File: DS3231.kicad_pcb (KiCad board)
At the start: 16 copper layers, 22.9 x 17.8 mm, 14 parts, among them IC1 DS3231/SO

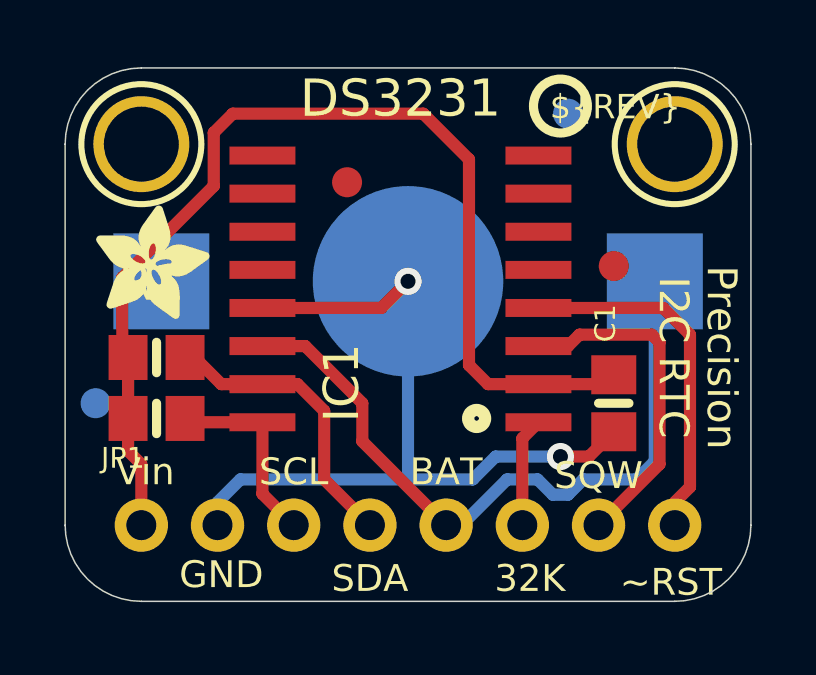
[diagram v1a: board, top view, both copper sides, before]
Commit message: fully migrated to KiCad
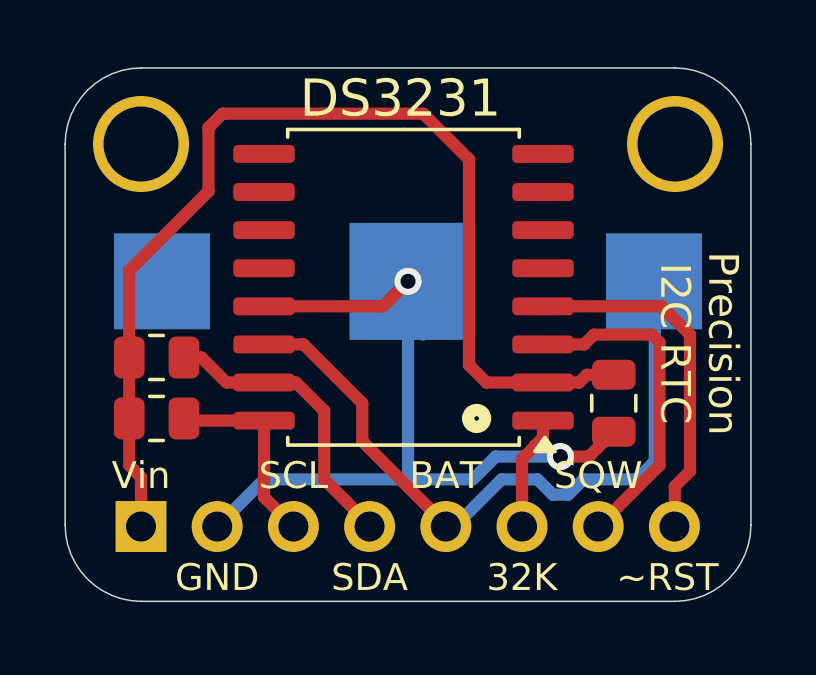
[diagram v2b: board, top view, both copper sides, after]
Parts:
- removed FID1, FID2, FID3, FID4: FIDUCIAL"", FIDUCIAL_1MM
- removed U$6, U$7: MOUNTINGHOLE2.5, MOUNTINGHOLE_2.5_PLATED
- removed U$8: , ADAFRUIT_3.5MM
- removed U$9: , PCBFEAT-REV-040
- added U$1: MOUNTINGHOLE2.5, MountingHole:MountingHole_2.5mm, F.Cu at (139.6, 98.7)
- added U$2: MOUNTINGHOLE2.5, MountingHole:MountingHole_2.5mm, F.Cu at (157.4, 98.7)
- B1: footprint CR1220 -> external_footprints:CR1220-SMD
- C1: footprint 0805-NO -> Capacitor_SMD:C_0805_2012Metric
- IC1: value DS3231/SO -> DS3231; footprint SO16W -> Package_SO:SOIC-16W_7.5x10.3mm_P1.27mm
- J1: renamed from JP1; value (none) -> Conn_01x08_Pin; footprint 1X08_ROUND_70 -> Connector_PinHeader_2.54mm:PinHeader_1x08_P2.54mm_Vertical; moved to B.Cu
- R1: renamed from R2; footprint 0805-NO -> Resistor_SMD:R_0805_2012Metric
- R2: renamed from R1; footprint 0805-NO -> Resistor_SMD:R_0805_2012Metric
- moved J1 8.90 mm to (139.6, 111.4), turned to -90 degrees
- moved IC1 0.12 mm to (148.3, 103.4), turned to 180 degrees
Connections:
- net 32KHZ renamed /32KHZ
- net SCL renamed /SCL
- net SDA renamed /SDA
- net SQW renamed /SQW
- net ~{RTC_RST} renamed /~{RTC_RST}
- IC1 pad 10: (no net) -> unconnected-(IC1-NC5-Pad10)
- IC1 pad 11: (no net) -> unconnected-(IC1-NC6-Pad11)
- IC1 pad 12: (no net) -> unconnected-(IC1-NC7-Pad12)
- IC1 pad 14: VBAT -> /VBAT
- IC1 pad 5: (no net) -> unconnected-(IC1-NC-Pad5)
- IC1 pad 6: (no net) -> unconnected-(IC1-NC1-Pad6)
- IC1 pad 7: (no net) -> unconnected-(IC1-NC2-Pad7)
- IC1 pad 8: (no net) -> unconnected-(IC1-NC3-Pad8)
- IC1 pad 9: (no net) -> unconnected-(IC1-NC4-Pad9)
- J1 pad 5: VBAT -> /VBAT
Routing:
- net VBAT: track 23.6 -> 0.00 mm
- net /VBAT: track 0.00 -> 23.6 mm

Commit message: fixed incorrect item in BOM
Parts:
- R1, R2: value 10K -> 10k

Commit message: updated routing + symbol update
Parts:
- J1: moved to F.Cu
- turned J1 to 90 degrees
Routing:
- net GND: track 28.6 -> 35.8 mm
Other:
- board text removed: "CR1220"
- board text removed: "Precision I2C RTC"

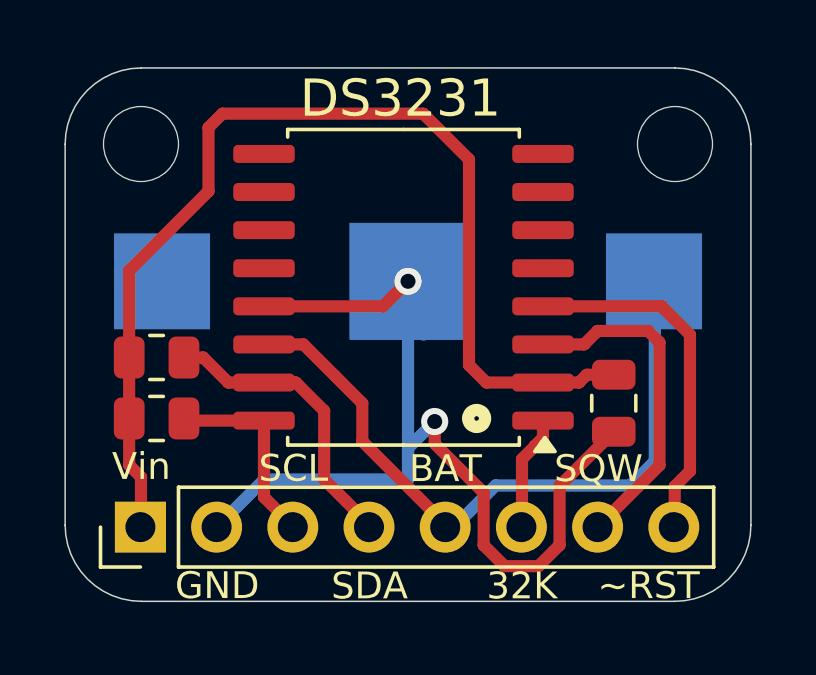
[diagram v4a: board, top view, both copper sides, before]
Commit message: silkscreen + routing update
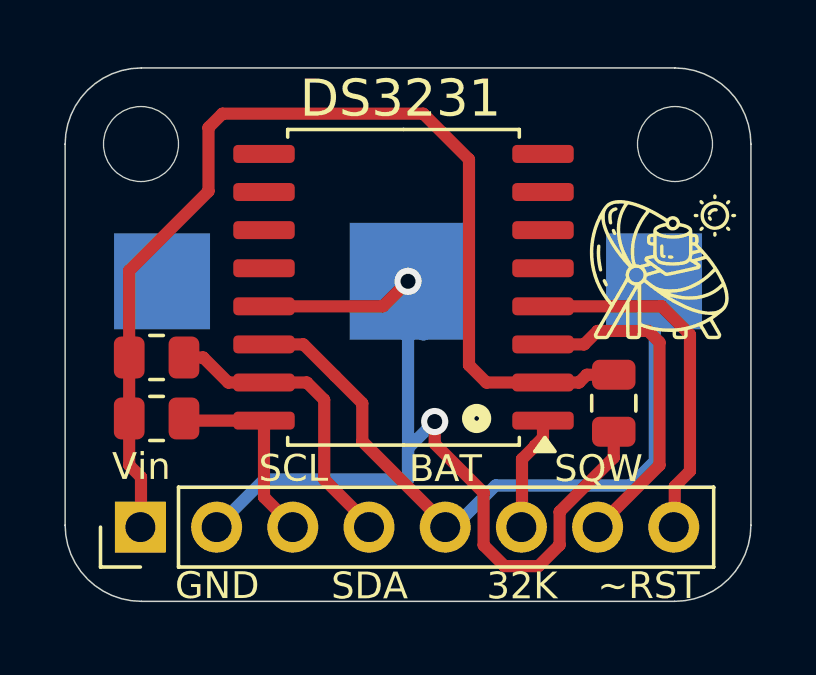
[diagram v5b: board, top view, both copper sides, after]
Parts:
- added G***: LOGO, external_footprints:logo, F.Cu at (157.0, 102.7)

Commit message: added ground plane front and bottom
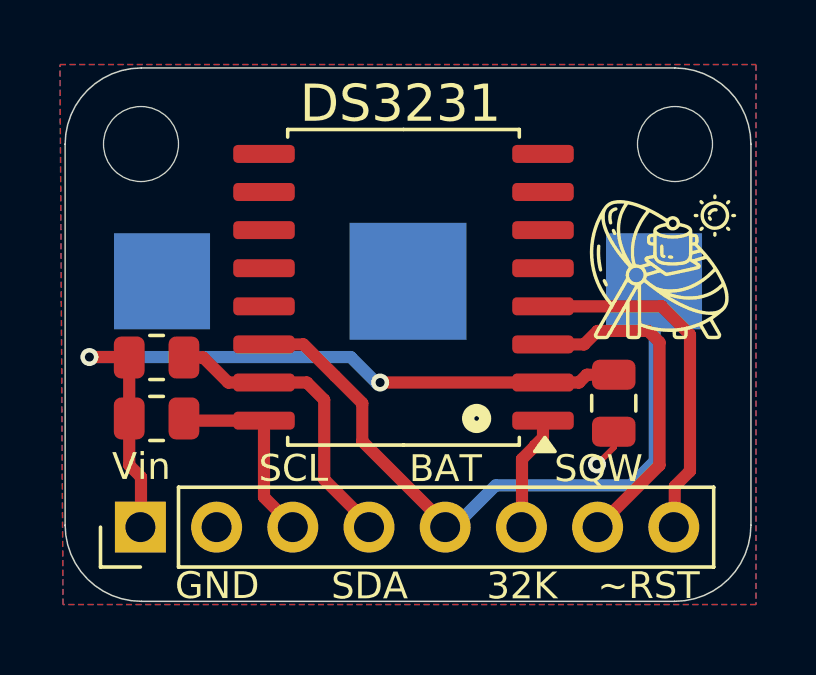
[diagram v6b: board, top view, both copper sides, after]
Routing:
- net GND: track 35.8 -> 1.32 mm, vias 2 -> 1
- net 3.3V: track 36.1 -> 25.1 mm, vias 0 -> 2
- added copper zone on B.Cu, net GND
- added copper zone on F.Cu, net GND
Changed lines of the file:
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@@
 	)
 	(gr_text "DS3231"
-		(at 148.2471 97.1296 0)
+		(at 148.2471 97.3 0)
 		(layer "F.SilkS")
 		(effects
@@
 	)
 	(segment
-		(start 152.85 112.72)
-		(end 151.72 112.72)
-		(width 0.4064)
+		(start 155.3591 108.2396)
+		(end 155.3591 108.7677)
+		(width 0.2)
 		(layer "F.Cu")
 		(net 1)
 	)
 	(segment
-		(start 153.5532 110.9068)
-		(end 153.5532 112.0168)
-		(width 0.4064)
+		(start 155.3591 108.7677)
+		(end 154.8 109.3268)
+		(width 0.2)
 		(layer "F.Cu")
 		(net 1)
 	)
-	(segment
-		(start 148.5011 103.2256)
-		(end 147.6671 104.0596)
-		(width 0.4064)
-		(layer "F.Cu")
-		(net 1)
-	)
-	(segment
-		(start 155.3591 109.1009)
-		(end 153.5532 110.9068)
-		(width 0.4064)
-		(layer "F.Cu")
-		(net 1)
-	)
-	(segment
-		(start 147.6671 104.0596)
-		(end 143.7 104.0596)
-		(width 0.4064)
-		(layer "F.Cu")
-		(net 1)
-	)
-	(segment
-		(start 155.3591 108.2396)
-		(end 155.3591 109.1009)
-		(width 0.4064)
-		(layer "F.Cu")
-		(net 1)
-	)
-	(segment
-		(start 151.72 112.72)
-		(end 151.02 112.02)
-		(width 0.4064)
-		(layer "F.Cu")
-		(net 1)
-	)
-	(segment
-		(start 151.02 112.02)
-		(end 151.02 110.27)
-		(width 0.4064)
-		(layer "F.Cu")
-		(net 1)
-	)
-	(segment
-		(start 153.5532 112.0168)
-		(end 152.85 112.72)
-		(width 0.4064)
-		(layer "F.Cu")
-		(net 1)
-	)
-	(segment
-		(start 149.39 108.64)
-		(end 149.39 107.9)
-		(width 0.4064)
-		(layer "F.Cu")
-		(net 1)
-	)
-	(segment
-		(start 151.02 110.27)
-		(end 149.39 108.64)
-		(width 0.4064)
-		(layer "F.Cu")
-		(net 1)
-	)
 	(via
-		(at 148.5011 103.2256)
-		(size 0.9064)
-		(drill 0.5)
+		(at 154.8 109.3268)
+		(size 0.6)
+		(drill 0.3)
 		(layers "F.Cu" "B.Cu")
 		(net 1)
 	)
-	(via
-		(at 149.39 107.9)
-		(size 0.9064)
-		(drill 0.5)
-		(layers "F.Cu" "B.Cu")
-		(net 1)
-	)
-	(segment
-		(start 149.0091 105.0036)
-		(end 149.0091 103.2256)
-		(width 0.4064)
-		(layer "B.Cu")
-		(net 1)
-	)
-	(segment
-		(start 143.7104 109.8296)
-		(end 142.1511 111.3889)
-		(width 0.4064)
-		(layer "B.Cu")
-		(net 1)
-	)
-	(segment
-		(start 148.5011 108.7889)
-		(end 148.5011 109.8296)
-		(width 0.4064)
-		(layer "B.Cu")
-		(net 1)
-	)
-	(segment
-		(start 149.0091 103.2256)
-		(end 148.5011 103.2256)
-		(width 0.4064)
-		(layer "B.Cu")
-		(net 1)
-	)
-	(segment
-		(start 142.1511 111.3889)
-		(end 142.1511 111.3536)
-		(width 0.4064)
-		(layer "B.Cu")
-		(net 1)
-	)
-	(segment
-		(start 148.5011 103.2256)
-		(end 148.5011 109.8296)
-		(width 0.4064)
-		(layer "B.Cu")
-		(net 1)
-	)
-	(segment
-		(start 149.39 107.9)
-		(end 148.5011 108.7889)
-		(width 0.4064)
-		(layer "B.Cu")
-		(net 1)
-	)
-	(segment
-		(start 148.5011 109.8296)
-		(end 143.7104 109.8296)
-		(width 0.4064)
-		(layer "B.Cu")
-		(net 1)
-	)
-	(segment
-		(start 150.5331 106.0196)
-		(end 150.5331 99.1616)
-		(width 0.4064)
-		(layer "F.Cu")
-		(net 2)
-	)
-	(segment
-		(start 142.3124 97.6376)
-		(end 141.85 98.1)
-		(width 0.4064)
-		(layer "F.Cu")
-		(net 2)
-	)
-	(segment
-		(start 150.5331 99.1616)
-		(end 149.0091 97.6376)
-		(width 0.4064)
-		(layer "F.Cu")
-		(net 2)
-	)
 	(segment
 		(start 139.6 109.75)
@@
 	)
 	(segment
-		(start 141.85 100.2247)
-		(end 139.2066 102.8681)
-		(width 0.4064)
-		(layer "F.Cu")
-		(net 2)
-	)
-	(segment
 		(start 154.4604 106.3396)
 		(end 154.2004 106.5996)
@@
 	)
 	(segment
-		(start 141.85 98.1)
-		(end 141.85 100.2247)
+		(start 147.5704 106.5996)
+		(end 153 106.5996)
+		(width 0.4064)
+		(layer "F.Cu")
+		(net 2)
+	)
+	(segment
+		(start 139.191 105.75)
+		(end 139.2066 105.7656)
 		(width 0.4064)
 		(layer "F.Cu")
@@
 	)
 	(segment
-		(start 151.1131 106.5996)
-		(end 153 106.5996)
-		(width 0.4064)
-		(layer "F.Cu")
-		(net 2)
-	)
-	(segment
 		(start 139.2066 105.7656)
 		(end 139.2066 107.7976)
@@
 	)
 	(segment
-		(start 139.2066 102.8681)
-		(end 139.2066 105.7656)
-		(width 0.4064)
-		(layer "F.Cu")
-		(net 2)
-	)
-	(segment
 		(start 154.2004 106.5996)
 		(end 153 106.5996)
@@
 	)
 	(segment
-		(start 149.0091 97.6376)
-		(end 142.3124 97.6376)
-		(width 0.4064)
-		(layer "F.Cu")
-		(net 2)
-	)
-	(segment
-		(start 151.1131 106.5996)
-		(end 150.5331 106.0196)
-		(width 0.4064)
-		(layer "F.Cu")
+		(start 137.88 105.75)
+		(end 139.191 105.75)
+		(width 0.4064)
+		(layer "F.Cu")
+		(net 2)
+	)
+	(via
+		(at 147.5704 106.5996)
+		(size 0.6)
+		(drill 0.3)
+		(layers "F.Cu" "B.Cu")
+		(net 2)
+	)
+	(via
+		(at 137.88 105.75)
+		(size 0.6)
+		(drill 0.3)
+		(layers "F.Cu" "B.Cu")
+		(net 2)
+	)
+	(segment
+		(start 146.59 105.75)
+		(end 137.88 105.75)
+		(width 0.4064)
+		(layer "B.Cu")
+		(net 2)
+	)
+	(segment
+		(start 147.4396 106.5996)
+		(end 146.59 105.75)
+		(width 0.4064)
+		(layer "B.Cu")
+		(net 2)
+	)
+	(segment
+		(start 147.5704 106.5996)
+		(end 147.4396 106.5996)
+		(width 0.4064)
+		(layer "B.Cu")
 		(net 2)
 	)
@@
 		(net 8)
 	)
+	(zone
+		(net 1)
+		(net_name "GND")
+		(layer "F.Cu")
+		(hatch edge 0.5)
+		(connect_pads
+			(clearance 0.5)
+		)
+		(min_thickness 0.25)
+		(filled_areas_thickness no)
+		(fill yes
+			(thermal_gap 0.5)
+			(thermal_bridge_width 0.5)
+		)
+		(polygon
+			(pts
+				(xy 160.1 96) (xy 160.1 114) (xy 137 114) (xy 136.9 96)
+			)
+		)
+	)
+	(zone
+		(net 1)
+		(net_name "GND")
+		(layer "B.Cu")
+		(hatch edge 0.5)
+		(connect_pads
+			(clearance 0.5)
+		)
+		(min_thickness 0.25)
+		(filled_areas_thickness no)
+		(fill yes
+			(thermal_gap 0.5)
+			(thermal_bridge_width 0.5)
+		)
+		(polygon
+			(pts
+				(xy 160.1 96) (xy 160.1 114) (xy 137 114) (xy 136.9 96)
+			)
+		)
+	)
 )

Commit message: production ready
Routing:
- net GND: track 1.32 -> 3.18 mm, vias 1 -> 2
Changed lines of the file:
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@@
 			)
 		)
+		(property ki_fp_filters "MountingHole*")
+		(sheetname "Root")
+		(sheetfile "DS3231.kicad_sch")
 		(attr exclude_from_pos_files exclude_from_bom)
 		(fp_circle
@@
 			)
 		)
+		(property ki_fp_filters "MountingHole*")
+		(sheetname "Root")
+		(sheetfile "DS3231.kicad_sch")
 		(attr exclude_from_pos_files exclude_from_bom)
 		(fp_circle
@@
 		(net 1)
 	)
+	(segment
+		(start 142.12 111.42)
+		(end 142.12 109.56)
+		(width 0.2)
+		(layer "F.Cu")
+		(net 1)
+	)
 	(via
 		(at 154.8 109.3268)
 		(size 0.6)
 		(drill 0.3)
+		(layers "F.Cu" "B.Cu")
+		(net 1)
+	)
+	(via
+		(at 142.12 109.56)
+		(size 0.6)
+		(drill 0.3)

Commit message: removed unused copper layers
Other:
- copper layers 16 -> 2
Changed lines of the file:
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@@
 	(layers
 		(0 "F.Cu" signal)
-		(1 "In1.Cu" signal)
-		(2 "In2.Cu" signal)
-		(3 "In3.Cu" signal)
-		(4 "In4.Cu" signal)
-		(5 "In5.Cu" signal)
-		(6 "In6.Cu" signal)
-		(7 "In7.Cu" signal)
-		(8 "In8.Cu" signal)
-		(9 "In9.Cu" signal)
-		(10 "In10.Cu" signal)
-		(11 "In11.Cu" signal)
-		(12 "In12.Cu" signal)
-		(13 "In13.Cu" signal)
-		(14 "In14.Cu" signal)
 		(31 "B.Cu" signal)
 		(32 "B.Adhes" user "B.Adhesive")
@@
 	)
 	(setup
+		(stackup
+			(layer "F.SilkS"
+				(type "Top Silk Screen")
+			)
+			(layer "F.Paste"
+				(type "Top Solder Paste")
+			)
+			(layer "F.Mask"
+				(type "Top Solder Mask")
+				(thickness 0.01)
+			)
+			(layer "F.Cu"
+				(type "copper")
+				(thickness 0.035)
+			)
+			(layer "dielectric 1"
+				(type "core")
+				(thickness 1.51)
+				(material "FR4")
+				(epsilon_r 4.5)
+				(loss_tangent 0.02)
+			)
+			(layer "B.Cu"
+				(type "copper")
+				(thickness 0.035)
+			)
+			(layer "B.Mask"
+				(type "Bottom Solder Mask")
+				(thickness 0.01)
+			)
+			(layer "B.Paste"
+				(type "Bottom Solder Paste")
+			)
+			(layer "B.SilkS"
+				(type "Bottom Silk Screen")
+			)
+			(copper_finish "None")
+			(dielectric_constraints no)
+		)
 		(pad_to_mask_clearance 0)
 		(allow_soldermask_bridges_in_footprints no)
